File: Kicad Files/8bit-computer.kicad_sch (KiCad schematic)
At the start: 50 parts, among them J1 USB_A

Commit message: alu rework start
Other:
- note added: "upgrade auf 74hc181 möglich"
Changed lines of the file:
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@@
     (effects (font (size 1.524 1.524)) (justify left bottom))
   )
+  (text "upgrade auf \n74hc181 möglich\n" (at 229.87 170.18 0)
+    (effects (font (size 1.524 1.524)) (justify left bottom))
+  )
   (text "built" (at 164.465 216.535 0)
     (effects (font (size 1.524 1.524)) (justify left bottom))
   )
+  (text "built" (at 98.425 76.835 0)
+    (effects (font (size 1.524 1.524)) (justify left bottom))
+  )
   (text "upgrade" (at 97.155 90.17 0)
     (effects (font (size 1.524 1.524)) (justify left bottom))
@@
       (reference "#PWR0133") (unit 1) (value "GND") (footprint "")
     )
+    (path "/00000000-0000-0000-0000-00005b5451db/5816edd0-db64-45f9-becd-0e1422d2c8da"
+      (reference "#PWR?") (unit 1) (value "VCC") (footprint "")
+    )
     (path "/00000000-0000-0000-0000-00005b57994f/e567e834-1d89-4569-93b8-8ce4a0f36bc2"
       (reference "#PWR?") (unit 1) (value "GND") (footprint "")
     )
+    (path "/00000000-0000-0000-0000-00005b5451db/f12bdbec-9b52-4df6-94cf-3f7c80d6acbf"
+      (reference "#PWR?") (unit 1) (value "VCC") (footprint "")
+    )
     (path "/00000000-0000-0000-0000-00005b64af9c"
       (reference "C1") (unit 1) (value "10µF") (footprint "Capacitor_THT:CP_Radial_D5.0mm_P2.00mm")
@@
       (reference "U67") (unit 1) (value "RP2040") (footprint "Package_DFN_QFN:QFN-56-1EP_7x7mm_P0.4mm_EP3.2x3.2mm")
     )
+    (path "/00000000-0000-0000-0000-00005b5451db/58e63b70-ab97-4aaa-beee-ecf7c395844b"
+      (reference "U?") (unit 1) (value "SST39SF020") (footprint "")
+    )
+    (path "/00000000-0000-0000-0000-00005b5451db/de317b5f-26bc-4061-8b8d-f0ac75510b6c"
+      (reference "U?") (unit 1) (value "SST39SF020") (footprint "")
+    )
   )

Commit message: np3
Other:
- sheet Control logic ports: added none; removed CEhb, CElb, CO, ~{Jhb}, ~{Jlb}
- note added: "not needed"

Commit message: np5
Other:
- sheet Output renamed Z register
- removed sheet Flags
- removed sheet Program counter
- sheet ALU ports: added CF, CLK, CLR, NF, OF, ZF, ~{FI}, Σ_0, Σ_1, Σ_2; removed Cin, Cout, E_0, E_1, E_2, E_3, E_4, E_5, E_6, E_7, SU
- sheet Control logic ports: added none; removed ~{CLR}
- sheet Z register: file output.kicad_sch -> Z register.kicad_sch

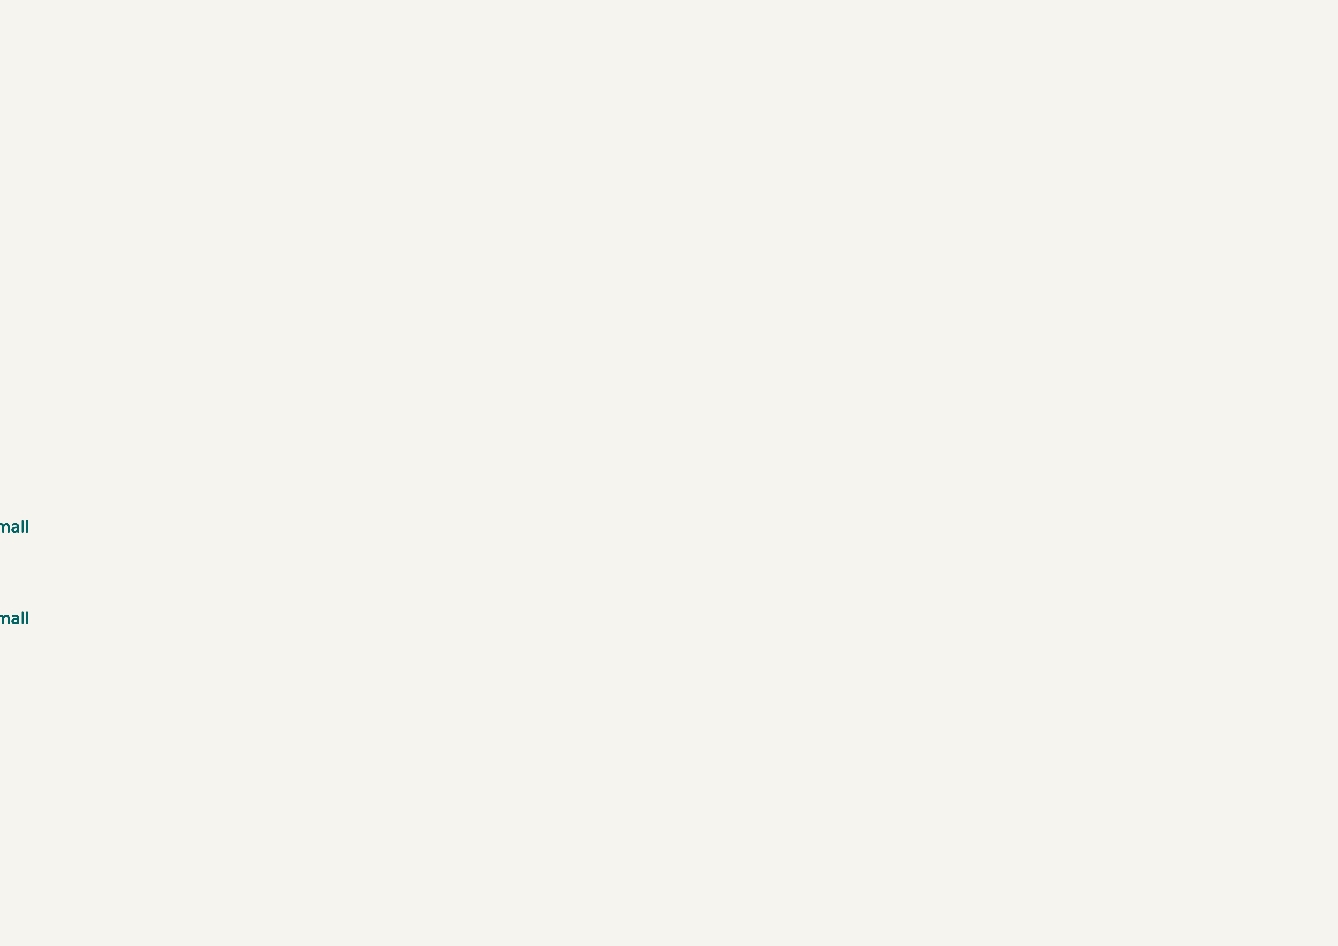
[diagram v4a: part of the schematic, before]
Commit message: added Flachband
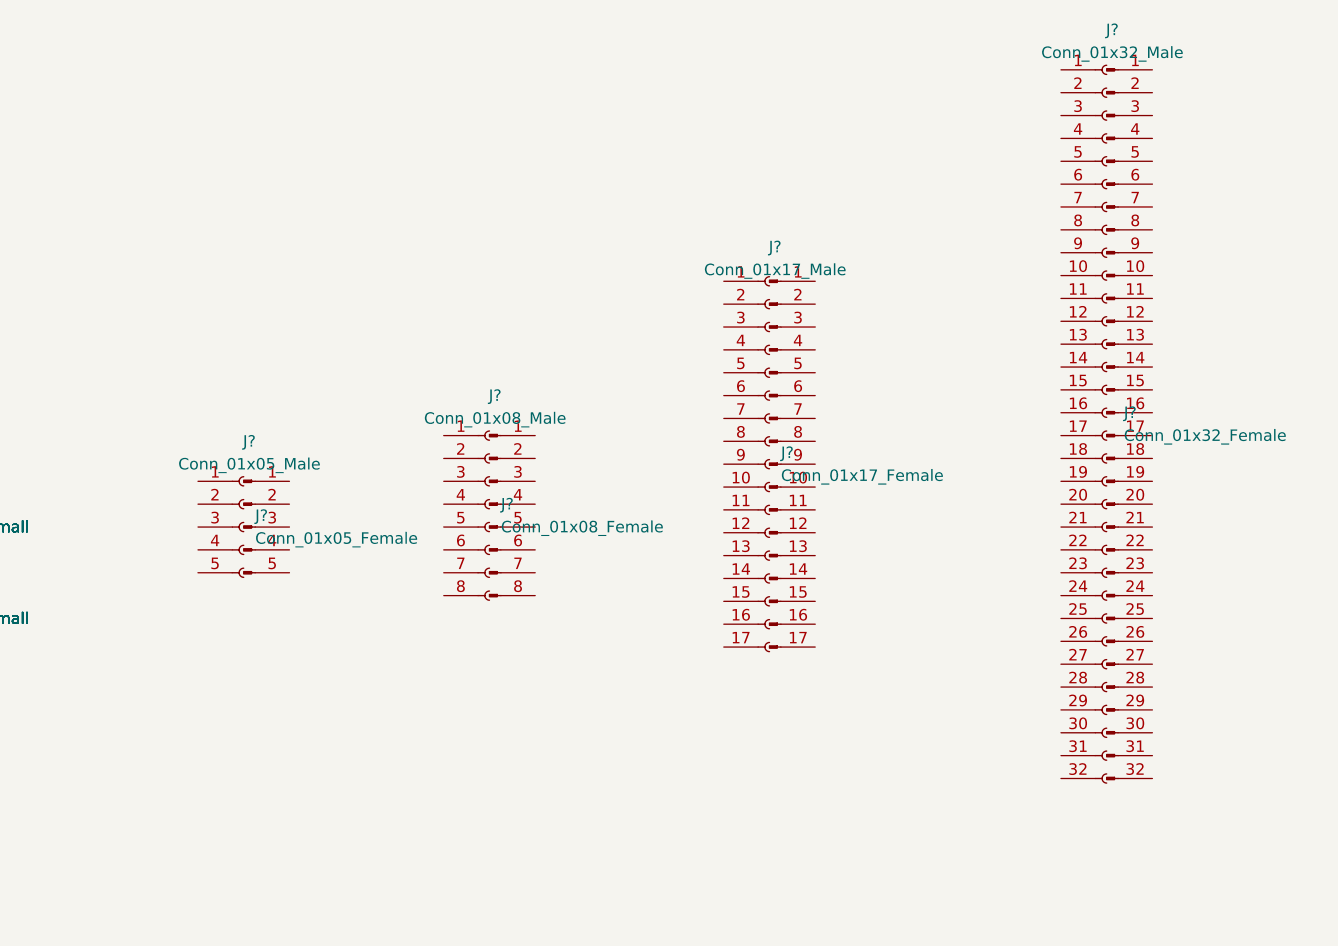
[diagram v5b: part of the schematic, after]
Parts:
- added J?: Conn_01x05_Female, symbol Connector:Conn_01x05_Female
- added J?: Conn_01x08_Male, symbol Connector:Conn_01x08_Male
- added J?: Conn_01x08_Female, symbol Connector:Conn_01x08_Female
- added J?: Conn_01x17_Female, symbol Connector:Conn_01x17_Female
- added J?: Conn_01x05_Male, symbol Connector:Conn_01x05_Male
- added J?: Conn_01x17_Male, symbol Connector:Conn_01x17_Male
- added J?: Conn_01x32_Female, symbol Connector:Conn_01x32_Female
- added J?: Conn_01x32_Male, symbol Connector:Conn_01x32_Male

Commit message: new control sigs
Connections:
- now unconnected: D1.2 (A), D10.2 (A), D11.2 (A), D12.2 (A), D13.2 (A), D14.2 (A), D15.2 (A), D16.2 (A), D17.2 (A), D18.2 (A), D19.2 (A), D2.2 (A), D20.2 (A), D21.2 (A), D22.2 (A), D23.2 (A), D24.2 (A), D3.2 (A), D4.2 (A), D5.2 (A), D6.2 (A), D7.2 (A), D8.2 (A), D9.2 (A)
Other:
- removed sheet A register
- removed sheet ALU
- removed sheet B register
- removed sheet Clock
- removed sheet Control logic
- removed sheet IO
- removed sheet Instruction register
- removed sheet MAR
- removed sheet RAM
- removed sheet X register
- removed sheet Y register
- removed sheet Z register
- added sheet A register1 (a-register.kicad_sch)
- added sheet ALU1 (alu.kicad_sch)
- added sheet B register1 (b-register.kicad_sch)
- added sheet Clock1 (clock.kicad_sch)
- added sheet Control logic1 (control.kicad_sch)
- added sheet IO1 (IO.kicad_sch)
- added sheet Instruction register1 (inst-register.kicad_sch)
- added sheet MAR1 (mar.kicad_sch)
- added sheet RAM1 (ram.kicad_sch)
- added sheet X register1 (x-register.kicad_sch)
- added sheet Y register1 (y-register.kicad_sch)
- added sheet Z register1 (Z register.kicad_sch)
- note added: "TODO: Tidy up Ctrl Word"
- note removed: "TODO:"
- note removed: "upgrade auf 74hc181 möglich"
- moved on the sheet: C1, J1

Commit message: tidy up
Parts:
- gave numbers to parts that had none: 8
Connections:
- net at D16.2 (A): now also D1.2 (A), D10.2 (A), D11.2 (A), D12.2 (A), D13.2 (A), D14.2 (A), D15.2 (A), D2.2 (A), D3.2 (A), D4.2 (A), D5.2 (A), D6.2 (A), D7.2 (A), D8.2 (A), D9.2 (A)
- net at D20.2 (A): now also D17.2 (A), D18.2 (A), D19.2 (A), D21.2 (A), D22.2 (A), D23.2 (A), D24.2 (A)
- net at J2.1 (Pin_1): now also J2.2 (Pin_2), J2.3 (Pin_3), J2.4 (Pin_4), J2.5 (Pin_5)
- net at J4.1 (Pin_1): now also J4.2 (Pin_2), J4.3 (Pin_3), J4.4 (Pin_4), J4.5 (Pin_5), J4.6 (Pin_6), J4.7 (Pin_7), J4.8 (Pin_8)
- net at J5.1 (Pin_1): now also J5.2 (Pin_2), J5.3 (Pin_3), J5.4 (Pin_4), J5.5 (Pin_5), J5.6 (Pin_6), J5.7 (Pin_7), J5.8 (Pin_8)
- net at J6.1 (Pin_1): now also J6.10 (Pin_10), J6.11 (Pin_11), J6.12 (Pin_12), J6.13 (Pin_13), J6.14 (Pin_14), J6.15 (Pin_15), J6.16 (Pin_16), J6.17 (Pin_17), J6.2 (Pin_2), J6.3 (Pin_3), J6.4 (Pin_4), J6.5 (Pin_5), J6.6 (Pin_6), J6.7 (Pin_7), J6.8 (Pin_8), J6.9 (Pin_9)
- net at J3.1 (Pin_1): now also J3.2 (Pin_2), J3.3 (Pin_3), J3.4 (Pin_4), J3.5 (Pin_5)
- net at J7.1 (Pin_1): now also J7.10 (Pin_10), J7.11 (Pin_11), J7.12 (Pin_12), J7.13 (Pin_13), J7.14 (Pin_14), J7.15 (Pin_15), J7.16 (Pin_16), J7.17 (Pin_17), J7.2 (Pin_2), J7.3 (Pin_3), J7.4 (Pin_4), J7.5 (Pin_5), J7.6 (Pin_6), J7.7 (Pin_7), J7.8 (Pin_8), J7.9 (Pin_9)
- net at J8.1 (Pin_1): now also J8.10 (Pin_10), J8.11 (Pin_11), J8.12 (Pin_12), J8.13 (Pin_13), J8.14 (Pin_14), J8.15 (Pin_15), J8.16 (Pin_16), J8.17 (Pin_17), J8.18 (Pin_18), J8.19 (Pin_19), J8.2 (Pin_2), J8.20 (Pin_20), J8.21 (Pin_21), J8.22 (Pin_22), J8.23 (Pin_23), J8.24 (Pin_24), J8.25 (Pin_25), J8.26 (Pin_26), J8.27 (Pin_27), J8.28 (Pin_28), J8.29 (Pin_29), J8.3 (Pin_3), J8.30 (Pin_30), J8.31 (Pin_31), J8.32 (Pin_32), J8.4 (Pin_4), J8.5 (Pin_5), J8.6 (Pin_6), J8.7 (Pin_7), J8.8 (Pin_8), J8.9 (Pin_9)
- net at J9.1 (Pin_1): now also J9.10 (Pin_10), J9.11 (Pin_11), J9.12 (Pin_12), J9.13 (Pin_13), J9.14 (Pin_14), J9.15 (Pin_15), J9.16 (Pin_16), J9.17 (Pin_17), J9.18 (Pin_18), J9.19 (Pin_19), J9.2 (Pin_2), J9.20 (Pin_20), J9.21 (Pin_21), J9.22 (Pin_22), J9.23 (Pin_23), J9.24 (Pin_24), J9.25 (Pin_25), J9.26 (Pin_26), J9.27 (Pin_27), J9.28 (Pin_28), J9.29 (Pin_29), J9.3 (Pin_3), J9.30 (Pin_30), J9.31 (Pin_31), J9.32 (Pin_32), J9.4 (Pin_4), J9.5 (Pin_5), J9.6 (Pin_6), J9.7 (Pin_7), J9.8 (Pin_8), J9.9 (Pin_9)
- no-connect marks 2 -> 11
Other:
- sheet A register1 renamed A register
- sheet ALU1 renamed ALU
- sheet B register1 renamed B register
- sheet Clock1 renamed Clock
- sheet Control logic1 renamed Control logic
- sheet IO1 renamed IO
- sheet Instruction register1 renamed Instruction register
- sheet MAR1 renamed MAR
- sheet RAM1 renamed RAM
- sheet X register1 renamed X register
- sheet Y register1 renamed Y register
- sheet Z register1 renamed Z register
- note added: "TODO: BOM"
- note removed: "TODO: Tidy up Ctrl Word"

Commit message: updated library
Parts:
- removed C1: 10µF, Capacitor_THT:CP_Radial_D5.0mm_P2.00mm, symbol 8bit-computer-rescue:CP1-Device
- added C1: C_Polarized, symbol Device:C_Polarized
- added D25, D26, D27, D28, D29, D30, D31, D32: LED, symbol Device:LED
- added R25, R26, R27, R28, R29, R30, R31, R32: R_Small, symbol Device:R_Small
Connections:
- net GND: now also C1.2, R25.2, R26.2, R27.2, R28.2, R29.2, R30.2, R31.2, R32.2
- net VCC: now also C1.1
- new net: D29.1 (K), R29.1
- new net: D32.1 (K), R32.1
- new net: D31.1 (K), R31.1
- new net: D25.2 (A), D26.2 (A), D27.2 (A), D28.2 (A), D29.2 (A), D30.2 (A), D31.2 (A), D32.2 (A)
- new net: D28.1 (K), R28.1
- new net: D27.1 (K), R27.1
- new net: D25.1 (K), R25.1
- new net: D30.1 (K), R30.1
- new net: D26.1 (K), R26.1
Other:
- sheet IO ports: added HLT; removed none
- moved on the sheet: J1
